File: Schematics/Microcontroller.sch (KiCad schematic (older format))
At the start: 26 parts, among them CON1 USB-MICRO-B, IC1 ATXMEGA256A3BU-A, J1 AVR_JTAG_Header, P1 CONN_02X08, SW1 SW_PUSH, SW2 SW_PUSH, SW3 SW_PUSH, SW4 SW_PUSH, X1 16MHz, X2 32.768KhZ

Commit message: Done lots of routing. Mostly done.
Rearranged some connections to make routing easier.
Need to check unconnected nets.
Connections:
- wire segments 139 -> 159
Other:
- moved on the sheet: SW1, SW2, SW3, SW4

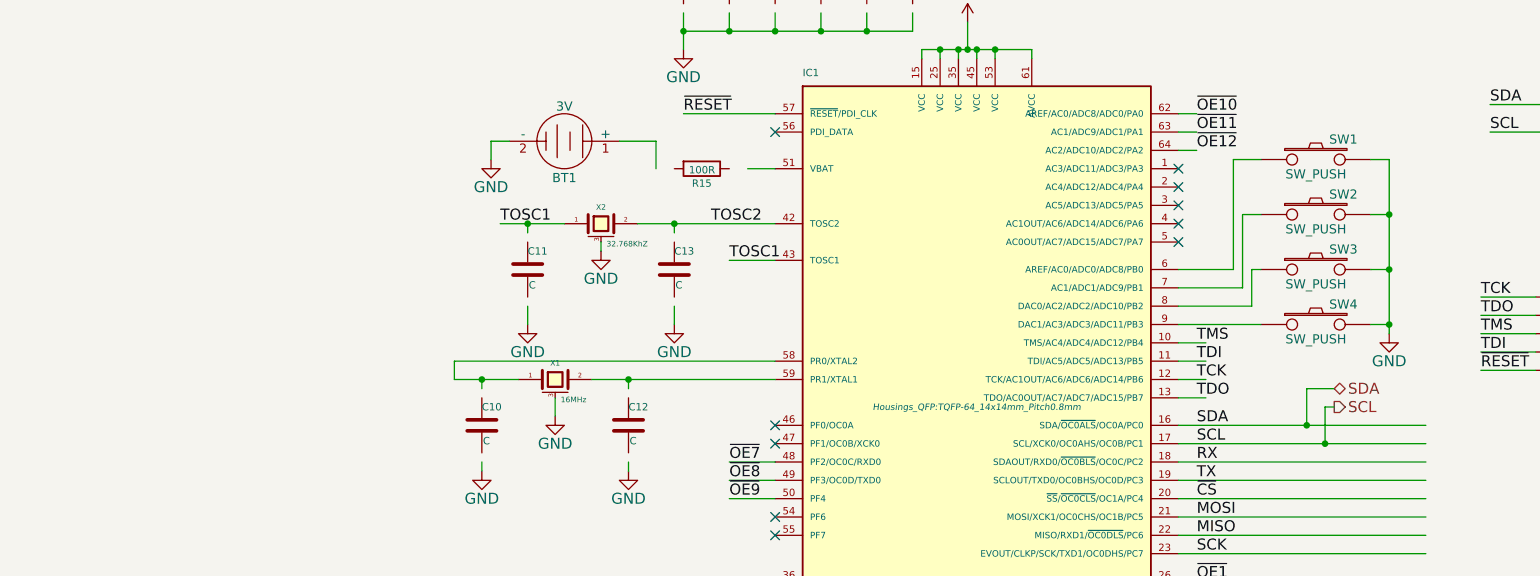
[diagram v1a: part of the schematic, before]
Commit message: Sorted silkscreen out. Added a select to change function of one of the switches to between a reset or a general purpose
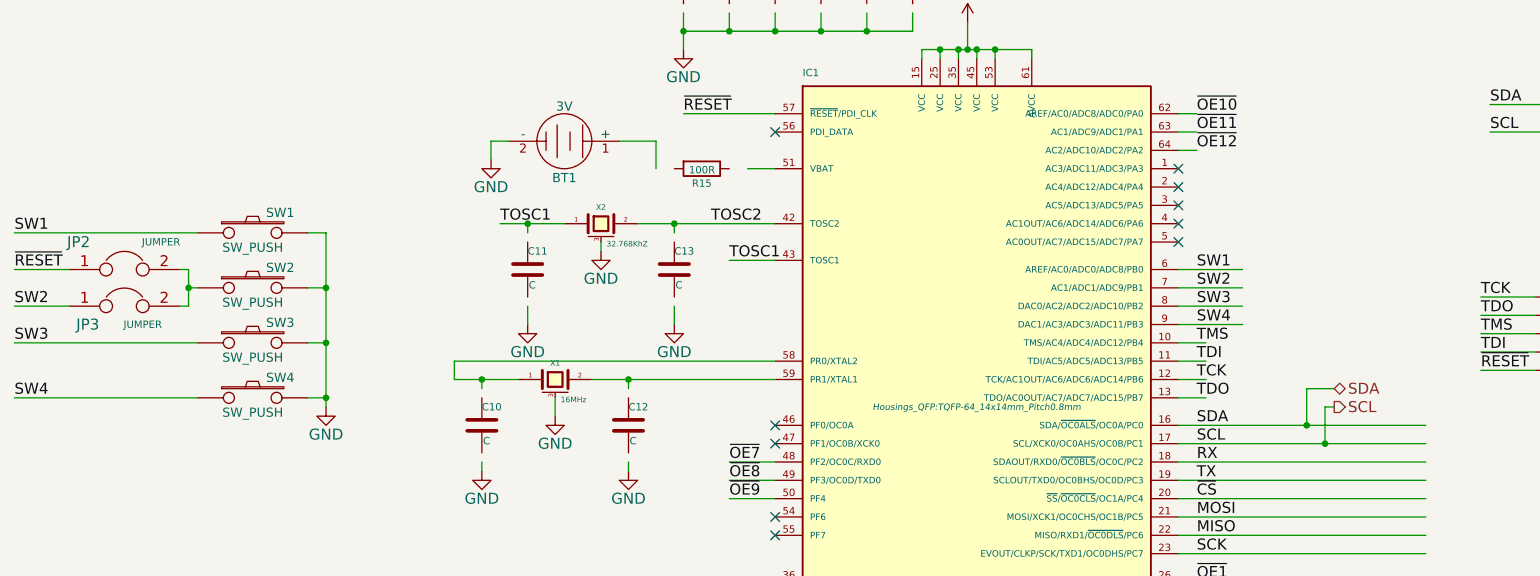
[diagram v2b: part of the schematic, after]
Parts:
- added JP2, JP3: JUMPER, Resistors_SMD:R_0603, symbol JUMPER
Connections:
- net labels added: SW1, SW2, SW3, SW4
- wire segments 159 -> 162
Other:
- moved on the sheet: SW1, SW2, SW3, SW4

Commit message: Completed layout of 10cm board. Fixes #8
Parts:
- C10, C12: value C -> 33pF
- C11, C13: value C -> 22pF
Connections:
- wire segments 162 -> 203
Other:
- note added: "Load capacitance of OSC pins = 3pF\n"
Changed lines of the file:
@@
 LIBS:pca9685
 LIBS:avr_jtag_header
-LIBS:linear-technology
 LIBS:Root-cache
 EELAYER 25 0
@@
 Text HLabel 4150 6550 2    60   Output ~ 0
 ~OE[1..12]
-Text HLabel 7800 3450 2    60   BiDi ~ 0
+Text HLabel 7400 3650 2    60   BiDi ~ 0
 SDA
-Text HLabel 7800 3550 2    60   Output ~ 0
+Text HLabel 7400 3750 2    60   Output ~ 0
 SCL
 Text Label 7050 3650 0    60   ~ 0
@@
 P 4200 2800
 F 0 "C13" H 4200 2900 40  0000 L CNN
-F 1 "C" H 4206 2715 40  0000 L CNN
+F 1 "22pF" H 4206 2715 40  0000 L CNN
 F 2 "Capacitors_SMD:C_0603" H 4238 2650 30  0001 C CNN
 F 3 "" H 4200 2800 60  0000 C CNN
@@
 P 3400 2800
 F 0 "C11" H 3400 2900 40  0000 L CNN
-F 1 "C" H 3406 2715 40  0000 L CNN
+F 1 "22pF" H 3406 2715 40  0000 L CNN
 F 2 "Capacitors_SMD:C_0603" H 3438 2650 30  0001 C CNN
 F 3 "" H 3400 2800 60  0000 C CNN
@@
 P 3950 3650
 F 0 "C12" H 3950 3750 40  0000 L CNN
-F 1 "C" H 3956 3565 40  0000 L CNN
+F 1 "33pF" H 3956 3565 40  0000 L CNN
 F 2 "Capacitors_SMD:C_0603" H 3988 3500 30  0001 C CNN
 F 3 "" H 3950 3650 60  0000 C CNN
@@
 P 3150 3650
 F 0 "C10" H 3150 3750 40  0000 L CNN
-F 1 "C" H 3156 3565 40  0000 L CNN
+F 1 "33pF" H 3156 3565 40  0000 L CNN
 F 2 "Capacitors_SMD:C_0603" H 3188 3500 30  0001 C CNN
 F 3 "" H 3150 3650 60  0000 C CNN
@@
 $EndComp
 Wire Wire Line
-	6950 3750 8300 3750
-Wire Wire Line
-	6950 3650 8300 3650
+	6950 3750 7350 3750
+Wire Wire Line
+	7350 3750 7350 3750
+Wire Wire Line
+	6950 3650 7400 3650
 Wire Wire Line
 	9400 1800 9400 2050
@@
 	9050 1900 9050 1800
 Wire Wire Line
-	9050 1300 9400 1300
+	9050 1300 9250 1300
+Wire Wire Line
+	9250 1300 9400 1300
 Wire Wire Line
 	9250 1300 9250 1200
@@
 	5550 1650 5550 1600
 Wire Wire Line
-	5550 1600 6150 1600
+	5550 1600 5650 1600
+Wire Wire Line
+	5650 1600 5750 1600
+Wire Wire Line
+	5750 1600 5800 1600
+Wire Wire Line
+	5800 1600 5850 1600
+Wire Wire Line
+	5850 1600 5950 1600
+Wire Wire Line
+	5950 1600 6150 1600
 Wire Wire Line
 	6150 1600 6150 1650
@@
 	5600 5500 5600 5550
 Wire Wire Line
-	5600 5550 6100 5550
+	5600 5550 5700 5550
+Wire Wire Line
+	5700 5550 5800 5550
+Wire Wire Line
+	5800 5550 5850 5550
+Wire Wire Line
+	5850 5550 5900 5550
+Wire Wire Line
+	5900 5550 6000 5550
+Wire Wire Line
+	6000 5550 6100 5550
 Wire Wire Line
 	6100 5550 6100 5500
@@
 Connection ~ 5850 5550
 Wire Bus Line
-	3200 5450 3200 6550
+	3200 5450 3200 5550
+Wire Bus Line
+	3200 5550 3200 5650
+Wire Bus Line
+	3200 5650 3200 5750
+Wire Bus Line
+	3200 5750 3200 5850
+Wire Bus Line
+	3200 5850 3200 5950
+Wire Bus Line
+	3200 5950 3200 6050
+Wire Bus Line
+	3200 6050 3200 6150
+Wire Bus Line
+	3200 6150 3200 6250
+Wire Bus Line
+	3200 6250 3200 6350
+Wire Bus Line
+	3200 6350 3200 6450
+Wire Bus Line
+	3200 6450 3200 6550
 Wire Bus Line
 	3200 6550 4150 6550
@@
 	8600 3350 8900 3350
 Wire Wire Line
-	9350 3600 9350 3750
+	9350 3600 9350 3650
+Wire Wire Line
+	9350 3650 9350 3750
 Wire Wire Line
 	9350 3650 9450 3650
@@
 	4250 1950 4750 1950
 Wire Wire Line
-	4000 2550 4750 2550
+	4000 2550 4200 2550
+Wire Wire Line
+	4200 2550 4750 2550
 Connection ~ 4200 2550
 Wire Wire Line
@@
 	3400 2600 3400 2550
 Wire Wire Line
-	3250 2550 3600 2550
+	3250 2550 3400 2550
+Wire Wire Line
+	3400 2550 3600 2550
 Connection ~ 3400 2550
 Wire Wire Line
@@
 	3150 3450 3150 3400
 Wire Wire Line
-	3000 3400 3350 3400
+	3000 3400 3150 3400
+Wire Wire Line
+	3150 3400 3350 3400
 Connection ~ 3150 3400
 Wire Wire Line
@@
 	3150 3900 3150 3850
 Wire Wire Line
-	3750 3400 4750 3400
+	3750 3400 3950 3400
+Wire Wire Line
+	3950 3400 4750 3400
 Wire Wire Line
 	3000 3300 4750 3300
@@
 	9050 5550 9400 5550
 Wire Wire Line
-	10450 5350 10450 5850
+	10450 5350 10450 5450
+Wire Wire Line
+	10450 5450 10450 5650
+Wire Wire Line
+	10450 5650 10450 5750
+Wire Wire Line
+	10450 5750 10450 5850
 Wire Wire Line
 	10450 5350 10400 5350
@@
 	9400 5650 9250 5650
 Wire Wire Line
-	9250 5650 9250 5850
+	9250 5650 9250 5750
+Wire Wire Line
+	9250 5750 9250 5850
 Wire Wire Line
 	9400 5750 9250 5750
@@
 	4250 1000 4250 950
 Wire Wire Line
-	4250 950  5500 950
+	4250 950  4500 950
+Wire Wire Line
+	4500 950  4750 950
+Wire Wire Line
+	4750 950  4900 950
+Wire Wire Line
+	4900 950  5000 950
+Wire Wire Line
+	5000 950  5250 950
+Wire Wire Line
+	5250 950  5500 950
 Wire Wire Line
 	5500 950  5500 1000
@@
 Connection ~ 4900 950
 Wire Wire Line
-	4250 1400 4250 1600
-Wire Wire Line
-	4250 1500 5500 1500
+	4250 1400 4250 1500
+Wire Wire Line
+	4250 1500 4250 1600
+Wire Wire Line
+	4250 1500 4500 1500
+Wire Wire Line
+	4500 1500 4750 1500
+Wire Wire Line
+	4750 1500 5000 1500
+Wire Wire Line
+	5000 1500 5250 1500
+Wire Wire Line
+	5250 1500 5500 1500
 Wire Wire Line
 	5500 1500 5500 1400
@@
 	9850 1900 9850 1850
 Wire Wire Line
-	9500 2450 9900 2450
+	9500 2450 9850 2450
+Wire Wire Line
+	9850 2450 9900 2450
 Wire Wire Line
 	9850 2400 9850 2450
@@
 	10550 2450 10500 2450
 Wire Wire Line
-	6950 3850 8300 3850
-Wire Wire Line
-	6950 3950 8300 3950
-Wire Wire Line
-	6950 4050 8300 4050
-Wire Wire Line
-	6950 4150 8300 4150
-Wire Wire Line
-	6950 4250 8300 4250
-Wire Wire Line
-	6950 4350 8300 4350
+	6950 3850 7350 3850
+Wire Wire Line
+	6950 3950 7350 3950
+Wire Wire Line
+	6950 4050 7350 4050
+Wire Wire Line
+	6950 4150 7350 4150
+Wire Wire Line
+	6950 4250 7350 4250
+Wire Wire Line
+	6950 4350 7350 4350
 Wire Wire Line
 	3000 3300 3000 3400
 Wire Wire Line
-	2300 5400 2300 6200
+	2300 5400 2300 5500
+Wire Wire Line
+	2300 5500 2300 5600
+Wire Wire Line
+	2300 5600 2300 5700
+Wire Wire Line
+	2300 5700 2300 5800
+Wire Wire Line
+	2300 5800 2300 5900
+Wire Wire Line
+	2300 5900 2300 6000
+Wire Wire Line
+	2300 6000 2300 6100
+Wire Wire Line
+	2300 6100 2300 6200
 Wire Wire Line
 	2200 5500 2300 5500
@@
 Connection ~ 2300 6100
 Wire Wire Line
-	7800 3550 7750 3550
-Wire Wire Line
-	7750 3550 7750 3750
-Connection ~ 7750 3750
-Wire Wire Line
-	7650 3450 7800 3450
-Wire Wire Line
-	7650 3450 7650 3650
-Connection ~ 7650 3650
+	7400 3750 7350 3750
+Wire Wire Line
+	7350 3750 7350 3750
 Wire Wire Line
 	6950 3100 7300 3100
@@
 	2200 2600 2300 2600
 Wire Wire Line
-	2300 2600 2300 3550
+	2300 2600 2300 2900
+Wire Wire Line
+	2300 2900 2300 3200
+Wire Wire Line
+	2300 3200 2300 3500
+Wire Wire Line
+	2300 3500 2300 3550
 Wire Wire Line
 	2200 3500 2300 3500
@@
 	1550 3000 1500 3000
 Wire Wire Line
-	1550 2800 1550 3000
+	1550 2800 1550 2900
+Wire Wire Line
+	1550 2900 1550 3000
 Wire Wire Line
 	1550 2900 1600 2900
@@
 Text Label 600  2800 0    60   ~ 0
 ~RESET
+Text Notes 1250 1300 0    60   ~ 0
+Load capacitance of OSC pins = 3pF\n
 $EndSCHEMATC

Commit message: Started Redesign.
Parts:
- SW1, SW2, SW3, SW4: footprint (none) -> rgb:SW
- renumbered P1 to P100
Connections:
- wire segments 203 -> 162

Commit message: Done some more layout.
Need to sort pin swaps for the OE lines and complete routing
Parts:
- removed P100: CONN_02X08, Socket_Strips:Socket_Strip_Straight_2x08, symbol CONN_02X08
- removed SW3, SW4: SW_PUSH, rgb:SW, symbol SW_PUSH
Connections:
- wire segments 162 -> 174
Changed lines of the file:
@@
 NoConn ~ 4750 3650
 NoConn ~ 6950 2450
-$Comp
-L CONN_02X08 P100
-U 1 1 54C8095F
-P 1950 5750
-F 0 "P100" H 1950 6200 50  0000 C CNN
-F 1 "CONN_02X08" V 1950 5750 50  0000 C CNN
-F 2 "Socket_Strips:Socket_Strip_Straight_2x08" H 1950 4550 60  0001 C CNN
-F 3 "" H 1950 4550 60  0000 C CNN
-	1    1950 5750
-	1    0    0    -1
-$EndComp
-$Comp
-L GND #PWR045
-U 1 1 54C80C62
-P 2300 6200
-F 0 "#PWR045" H 2300 5950 60  0001 C CNN
-F 1 "GND" H 2300 6050 60  0000 C CNN
-F 2 "" H 2300 6200 60  0000 C CNN
-F 3 "" H 2300 6200 60  0000 C CNN
-	1    2300 6200
-	1    0    0    -1
-$EndComp
 NoConn ~ 9400 5350
 $Comp
@@
 	9050 1700 9050 1900
 Wire Wire Line
-	9050 1300 9400 1300
+	9050 1300 9250 1300
+Wire Wire Line
+	9250 1300 9400 1300
 Wire Wire Line
 	9250 1300 9250 1200
@@
 	5550 1650 5550 1600
 Wire Wire Line
-	5550 1600 6150 1600
+	5550 1600 5650 1600
+Wire Wire Line
+	5650 1600 5750 1600
+Wire Wire Line
+	5750 1600 5800 1600
+Wire Wire Line
+	5800 1600 5850 1600
+Wire Wire Line
+	5850 1600 5950 1600
+Wire Wire Line
+	5950 1600 6150 1600
 Wire Wire Line
 	6150 1600 6150 1650
@@
 	5600 5500 5600 5550
 Wire Wire Line
-	5600 5550 6100 5550
+	5600 5550 5700 5550
+Wire Wire Line
+	5700 5550 5800 5550
+Wire Wire Line
+	5800 5550 5850 5550
+Wire Wire Line
+	5850 5550 5900 5550
+Wire Wire Line
+	5900 5550 6000 5550
+Wire Wire Line
+	6000 5550 6100 5550
 Wire Wire Line
 	6100 5550 6100 5500
@@
 Connection ~ 5850 5550
 Wire Bus Line
-	3200 5450 3200 6550
+	3200 5450 3200 5550
+Wire Bus Line
+	3200 5550 3200 5650
+Wire Bus Line
+	3200 5650 3200 5750
+Wire Bus Line
+	3200 5750 3200 5850
+Wire Bus Line
+	3200 5850 3200 5950
+Wire Bus Line
+	3200 5950 3200 6050
+Wire Bus Line
+	3200 6050 3200 6150
+Wire Bus Line
+	3200 6150 3200 6250
+Wire Bus Line
+	3200 6250 3200 6350
+Wire Bus Line
+	3200 6350 3200 6450
+Wire Bus Line
+	3200 6450 3200 6550
 Wire Bus Line
 	3200 6550 4150 6550
@@
 	8600 3350 8900 3350
 Wire Wire Line
-	9350 3600 9350 3750
+	9350 3600 9350 3650
+Wire Wire Line
+	9350 3650 9350 3750
 Wire Wire Line
 	9350 3650 9450 3650
@@
 	4250 1950 4750 1950
 Wire Wire Line
-	4000 2550 4750 2550
+	4000 2550 4200 2550
+Wire Wire Line
+	4200 2550 4750 2550
 Connection ~ 4200 2550
 Wire Wire Line
@@
 	3400 2550 3400 2650
 Wire Wire Line
-	3250 2550 3600 2550
+	3250 2550 3400 2550
+Wire Wire Line
+	3400 2550 3600 2550
 Connection ~ 3400 2550
 Wire Wire Line
@@
 	3150 3400 3150 3500
 Wire Wire Line
-	3000 3400 3350 3400
+	3000 3400 3150 3400
+Wire Wire Line
+	3150 3400 3350 3400
 Connection ~ 3150 3400
 Wire Wire Line
@@
 	3150 3800 3150 3900
 Wire Wire Line
-	3750 3400 4750 3400
+	3750 3400 3950 3400
+Wire Wire Line
+	3950 3400 4750 3400
 Wire Wire Line
 	3000 3300 4750 3300
@@
 	9050 5550 9400 5550
 Wire Wire Line
-	10450 5350 10450 5850
+	10450 5350 10450 5450
+Wire Wire Line
+	10450 5450 10450 5650
+Wire Wire Line
+	10450 5650 10450 5750
+Wire Wire Line
+	10450 5750 10450 5850
 Wire Wire Line
 	10450 5350 10400 5350
@@
 	9400 5650 9250 5650
 Wire Wire Line
-	9250 5650 9250 5850
+	9250 5650 9250 5750
+Wire Wire Line
+	9250 5750 9250 5850
 Wire Wire Line
 	9400 5750 9250 5750
@@
 	4250 950  4250 1050
 Wire Wire Line
-	4250 950  5500 950
+	4250 950  4500 950
+Wire Wire Line
+	4500 950  4750 950
+Wire Wire Line
+	4750 950  4900 950
+Wire Wire Line
+	4900 950  5000 950
+Wire Wire Line
+	5000 950  5250 950
+Wire Wire Line
+	5250 950  5500 950
 Wire Wire Line
 	5500 950  5500 1050
@@
 Connection ~ 4900 950
 Wire Wire Line
-	4250 1350 4250 1600
-Wire Wire Line
-	5500 1500 4250 1500
+	4250 1350 4250 1500
+Wire Wire Line
+	4250 1500 4250 1600
+Wire Wire Line
+	5500 1500 5250 1500
+Wire Wire Line
+	5250 1500 5000 1500
+Wire Wire Line
+	5000 1500 4750 1500
+Wire Wire Line
+	4750 1500 4500 1500
+Wire Wire Line
+	4500 1500 4250 1500
 Wire Wire Line
 	5500 1350 5500 1500
@@
 	9850 1850 9850 2000
 Wire Wire Line
-	9500 2450 9900 2450
+	9500 2450 9850 2450
+Wire Wire Line
+	9850 2450 9900 2450
 Wire Wire Line
 	9850 2300 9850 2450
@@
 	3000 3300 3000 3400
 Wire Wire Line
-	2300 5400 2300 6200
-Wire Wire Line
-	2200 5500 2300 5500
-Connection ~ 2300 5500
-Wire Wire Line
-	2300 5600 2200 5600
-Connection ~ 2300 5600
-Wire Wire Line
-	2200 5700 2300 5700
-Connection ~ 2300 5700
-Wire Wire Line
-	2300 5800 2200 5800
-Connection ~ 2300 5800
-Wire Wire Line
-	2200 5900 2300 5900
-Connection ~ 2300 5900
-Wire Wire Line
-	2300 6000 2200 6000
-Connection ~ 2300 6000
-Wire Wire Line
-	2200 6100 2300 6100
-Connection ~ 2300 6100
-Wire Wire Line
 	7350 3750 7350 3750
 Wire Wire Line
@@
 	2200 2600 2300 2600
 Wire Wire Line
-	2300 2600 2300 3550
-Wire Wire Line
-	2200 3500 2300 3500
-Connection ~ 2300 3500
-Wire Wire Line
-	2200 3200 2300 3200
-Connection ~ 2300 3200
+	2300 2600 2300 2900
+Wire Wire Line
+	2300 2900 2300 3050
 Wire Wire Line
 	2200 2900 2300 2900
 Connection ~ 2300 2900
-$Comp
-L GND #PWR046
-U 1 1 54C97F8A
-P 2300 3550
-F 0 "#PWR046" H 2300 3300 60  0001 C CNN
-F 1 "GND" H 2300 3400 60  0000 C CNN
-F 2 "" H 2300 3550 60  0000 C CNN
-F 3 "" H 2300 3550 60  0000 C CNN
-	1    2300 3550
-	1    0    0    -1
-$EndComp
 $Comp
 L SW_PUSH SW2
@@
 F 5 "Farnell" H 1900 2900 60  0001 C CNN "Supplier"
 	1    1900 2900
-	1    0    0    -1
-$EndComp
-$Comp
-L SW_PUSH SW3
-U 1 1 54C9B54A
-P 1900 3200
-F 0 "SW3" H 2050 3310 50  0000 C CNN
-F 1 "SW_PUSH" H 1900 3120 50  0000 C CNN
-F 2 "rgb:SW" H 1900 3200 60  0001 C CNN
-F 3 "http://www.newark.com/pdfs/datasheets/spc/Ta-1143.pdf" H 1900 3200 60  0001 C CNN
-F 4 "MC32882" H 1900 3200 60  0001 C CNN "Part"
-F 5 "Farnell" H 1900 3200 60  0001 C CNN "Supplier"
-	1    1900 3200
-	1    0    0    -1
-$EndComp
-$Comp
-L SW_PUSH SW4
-U 1 1 54C9B587
-P 1900 3500
-F 0 "SW4" H 2050 3610 50  0000 C CNN
-F 1 "SW_PUSH" H 1900 3420 50  0000 C CNN
-F 2 "rgb:SW" H 1900 3500 60  0001 C CNN
-F 3 "http://www.newark.com/pdfs/datasheets/spc/Ta-1143.pdf" H 1900 3500 60  0001 C CNN
-F 4 "MC32882" H 1900 3500 60  0001 C CNN "Part"
-F 5 "Farnell" H 1900 3500 60  0001 C CNN "Supplier"
-	1    1900 3500
 	1    0    0    -1
 $EndComp
@@
 NoConn ~ 6950 2350
 NoConn ~ 6950 2250
-Wire Wire Line
-	2200 5400 2300 5400
-Text Label 1450 5400 0    60   ~ 0
-SDA
-Text Label 1450 5500 0    60   ~ 0
-SCL
-Text Label 1450 6100 0    60   ~ 0
-RX
-Text Label 1450 6000 0    60   ~ 0
-TX
-Text Label 1450 5900 0    60   ~ 0
-~CS
-Text Label 1450 5800 0    60   ~ 0
-MOSI
-Text Label 1450 5700 0    60   ~ 0
-MISO
-Text Label 1450 5600 0    60   ~ 0
-SCK
-Wire Wire Line
-	1450 5400 1700 5400
-Wire Wire Line
-	1700 5500 1450 5500
-Wire Wire Line
-	1450 5600 1700 5600
-Wire Wire Line
-	1700 5700 1450 5700
-Wire Wire Line
-	1450 5800 1700 5800
-Wire Wire Line
-	1700 5900 1450 5900
-Wire Wire Line
-	1450 6000 1700 6000
-Wire Wire Line
-	1700 6100 1450 6100
 $Comp
 L JUMPER JP3
@@
 	1550 3000 1500 3000
 Wire Wire Line
-	1550 2800 1550 3000
+	1550 2800 1550 2900
+Wire Wire Line
+	1550 2900 1550 3000
 Wire Wire Line
 	1550 2900 1600 2900
@@
 	1500 2800 1550 2800
 Connection ~ 1550 2900
-Wire Wire Line
-	1600 3200 600  3200
-Wire Wire Line
-	1600 3500 600  3500
 Text Label 600  2600 0    60   ~ 0
 SW1
 Text Label 600  3000 0    60   ~ 0
 SW2
-Text Label 600  3200 0    60   ~ 0
-SW3
-Text Label 600  3500 0    60   ~ 0
-SW4
 Text Label 600  2800 0    60   ~ 0
 ~RESET
@@
 Wire Wire Line
 	9400 1300 9400 1400
+$Comp
+L GND #PWR046
+U 1 1 54C97F8A
+P 2300 3050
+F 0 "#PWR046" H 2300 2800 60  0001 C CNN
+F 1 "GND" H 2300 2900 60  0000 C CNN
+F 2 "" H 2300 3050 60  0000 C CNN
+F 3 "" H 2300 3050 60  0000 C CNN
+	1    2300 3050
+	1    0    0    -1
+$EndComp
 $EndSCHEMATC
